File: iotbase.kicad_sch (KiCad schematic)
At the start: 35 parts, among them J1 USB_C_Receptacle_USB2.0, J2 RCWL-0516, J3 HSPI, J4 VSPI, SW1 Reset, SW2 Boot, U1 AMS1117-3.3, U2 Connector_IoT_GPIO, U3 ESP32-WROOM-E, U4 BME280, U6 Connector_ESProg, U7 Connector_I2C, U8 Connector_I2C

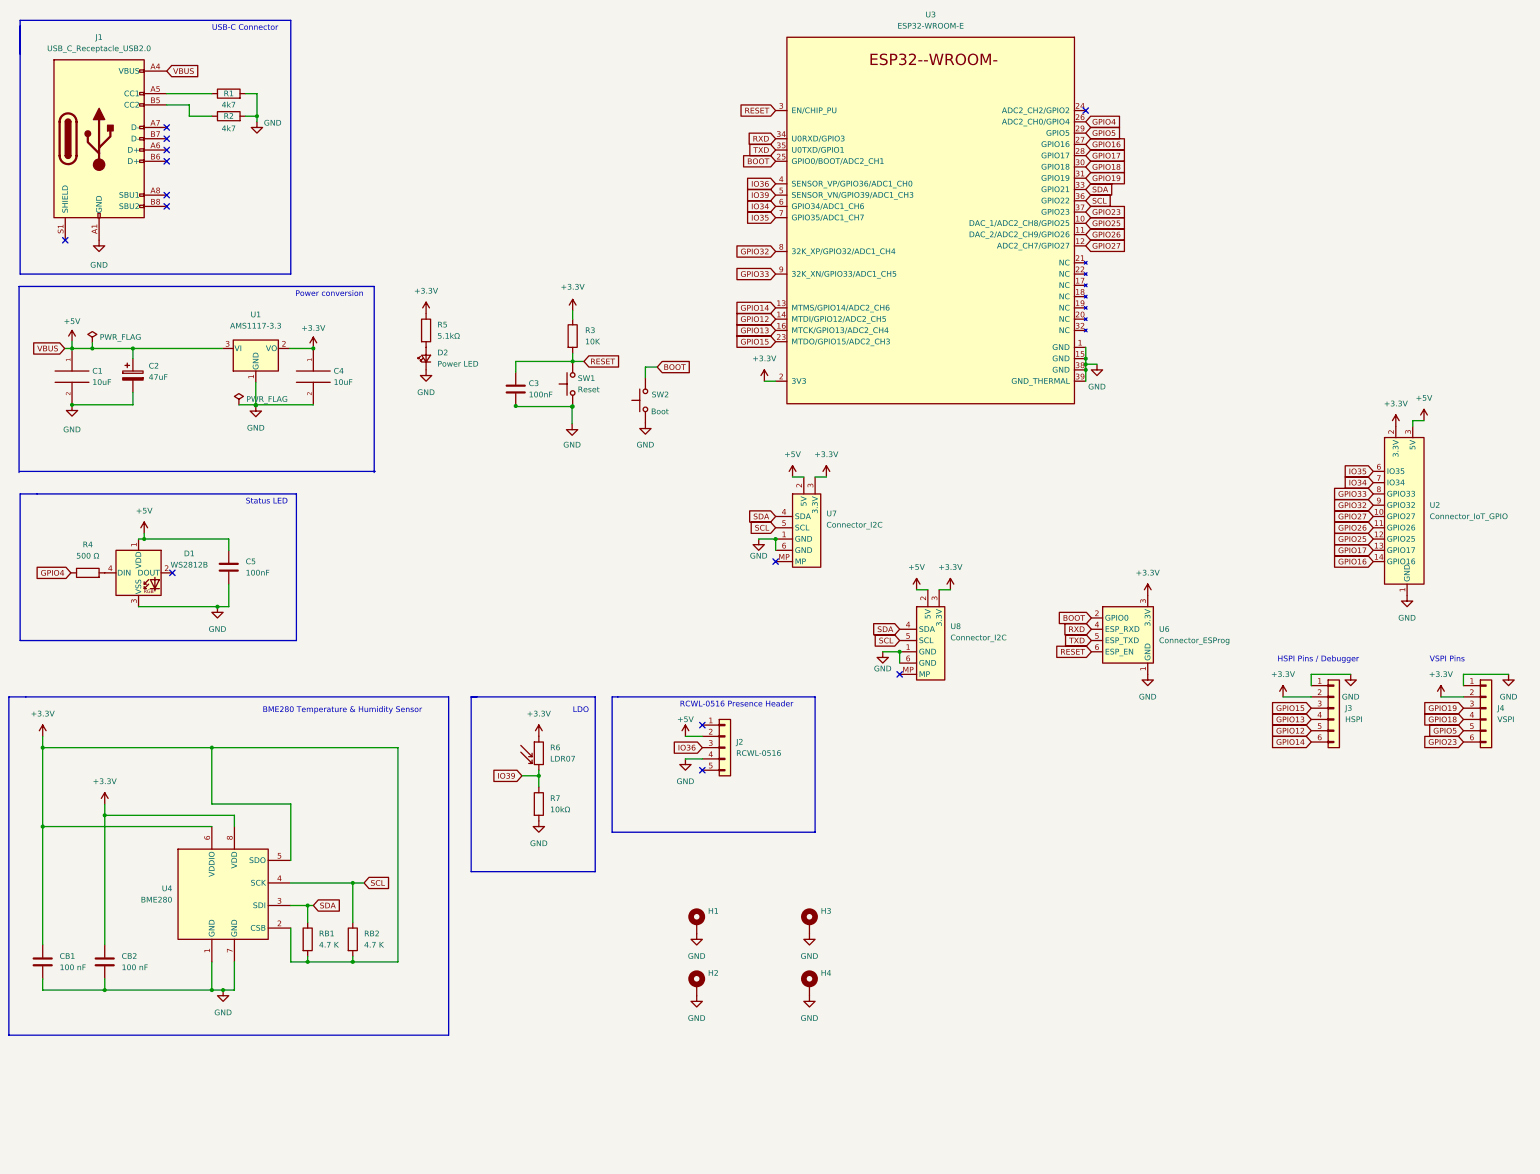
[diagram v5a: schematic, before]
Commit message: updated components and layout.
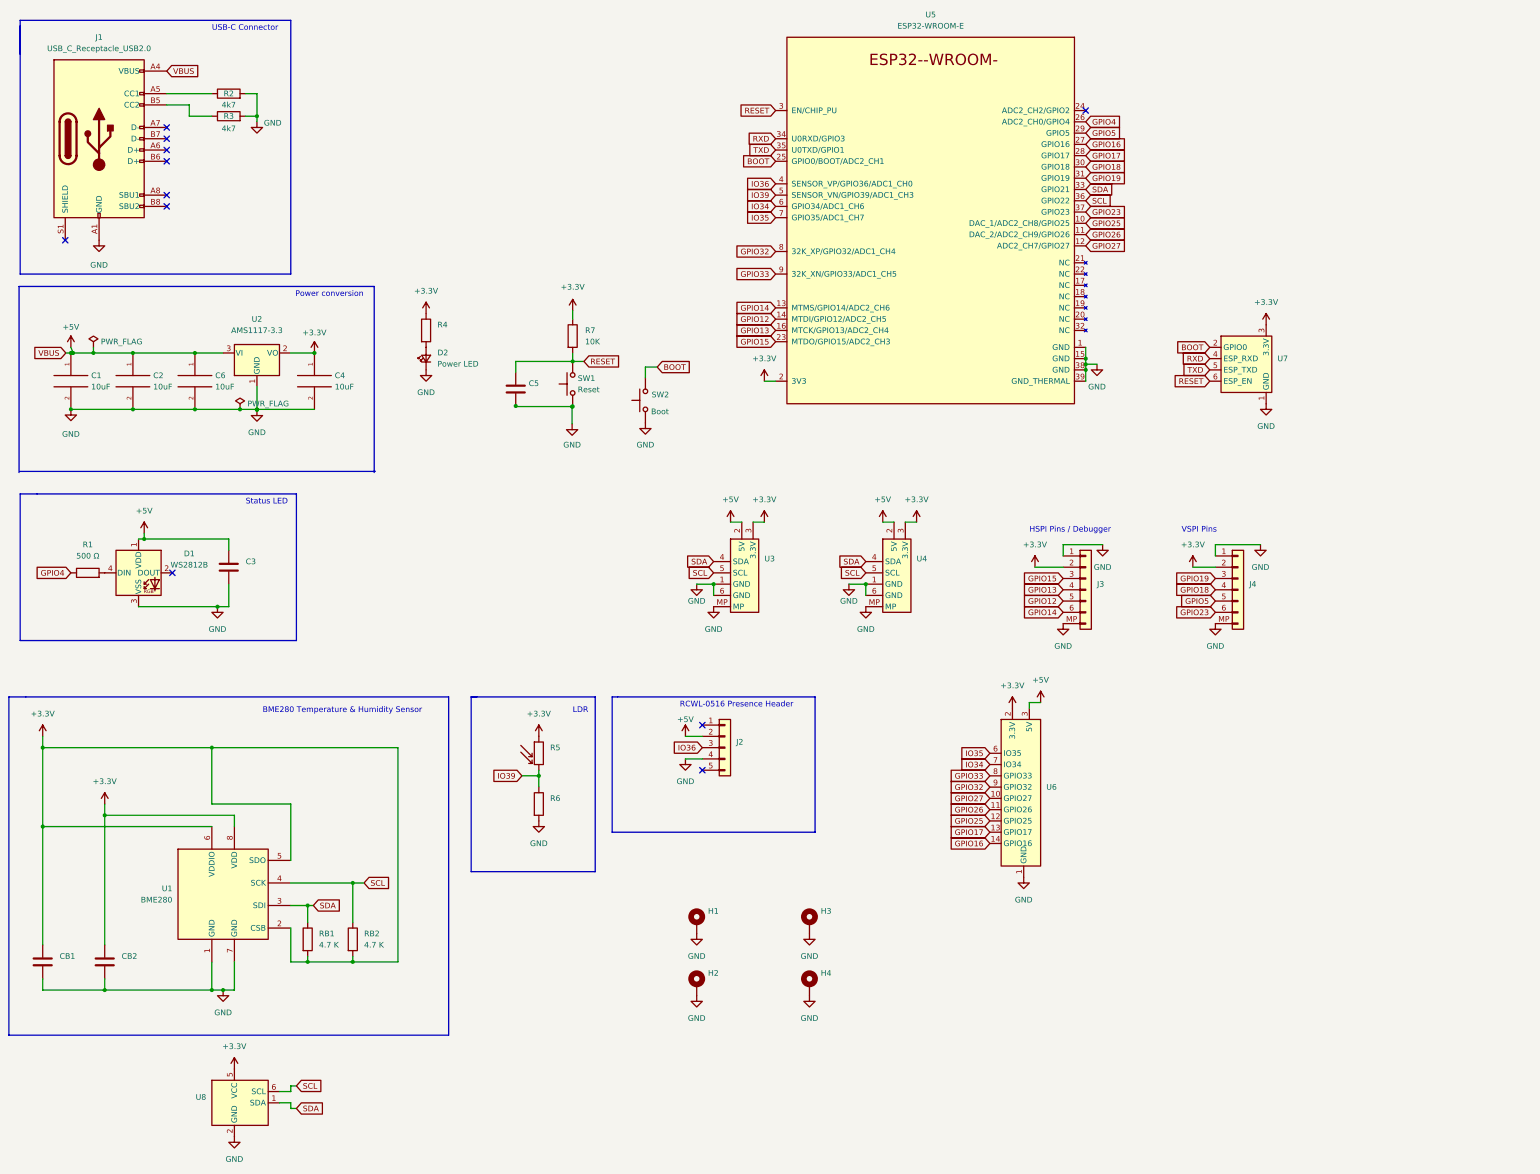
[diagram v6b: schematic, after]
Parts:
- removed C2: 47uF, Capacitor_SMD:C_1206_3216Metric, symbol Device:C_Polarized
- removed J3: HSPI, Connector_JST:JST_SH_BM06B-SRSS-TB_1x06-1MP_P1.00mm_Vertical, symbol Connector_Generic:Conn_01x06
- removed J4: VSPI, Connector_JST:JST_SH_BM06B-SRSS-TB_1x06-1MP_P1.00mm_Vertical, symbol Connector_Generic:Conn_01x06
- added C2, C6: 10uF, Capacitor_SMD:C_0603_1608Metric, symbol pspice:CAP
- added J3, J4: (no value), symbol Connector_Generic:Conn_01x07
- added U8: (no value), symbol Sensor_Humidity:HDC1080
- C3: renamed from C5; value 100nF -> (none); footprint Resistor_SMD:R_0603_1608Metric -> (none)
- C5: renamed from C3; value 100nF -> (none); footprint Resistor_SMD:R_0603_1608Metric -> (none)
- CB1, CB2: value 100 nF -> (none)
- J2: value RCWL-0516 -> (none); footprint 0_Project:PinHeader_RCWL-0516 -> (none); now left out of the parts list
- R4: renamed from R5; value 5.1kΩ -> (none)
- R5: renamed from R6; value LDR07 -> (none); footprint OptoDevice:R_LDR_5.1x4.3mm_P3.4mm_Vertical -> (none); now left out of the parts list
- R6: renamed from R7; value 10kΩ -> (none)
- U3: renamed from U7; value Connector_I2C -> (none); footprint Connector_JST:JST_SH_BM06B-SRSS-TB_1x06-1MP_P1.00mm_Vertical -> (none); now left out of the parts list
- U4: renamed from U8; value Connector_I2C -> (none); footprint Connector_JST:JST_SH_BM06B-SRSS-TB_1x06-1MP_P1.00mm_Vertical -> (none); now left out of the parts list
- U6: renamed from U2; value Connector_IoT_GPIO -> (none); footprint 0_Project:Connector_IoT_GPIO -> (none)
- U7: renamed from U6; value Connector_ESProg -> (none); footprint Connector:Tag-Connect_TC2030-IDC-FP_2x03_P1.27mm_Vertical -> (none); now left out of the parts list
- renumbered R4 to R1, R1 to R2, R2 to R3, R3 to R7, U4 to U1, U1 to U2, U3 to U5
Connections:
- net +3V3: now also J3.2 (Pin_2), J4.2 (Pin_2), U8.5 (VCC)
- net +5V: now also C2.1, C6.1
- net GND: now also U3.MP, U4.MP, C2.2, C6.2, J3.1 (Pin_1), J3.MP, J4.1 (Pin_1), J4.MP, U8.2 (GND)
- net GPIO12: now also J3.5 (Pin_5)
- net GPIO13: now also J3.4 (Pin_4)
- net GPIO14: now also J3.6 (Pin_6)
- net GPIO15: now also J3.3 (Pin_3)
- net GPIO18: now also J4.4 (Pin_4)
- net GPIO19: now also J4.3 (Pin_3)
- net GPIO23: now also J4.6 (Pin_6)
- net GPIO5: now also J4.5 (Pin_5)
- net SCL: now also U8.6 (SCL)
- net SDA: now also U8.1 (SDA)
- no-connect marks 13 -> 11
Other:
- note added: "LDR"
- note removed: "LDO"
- moved on the sheet: C1, C4, U2, U3, U4, U6, U7

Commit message: adds rounded corners adds connector pin silkscreens
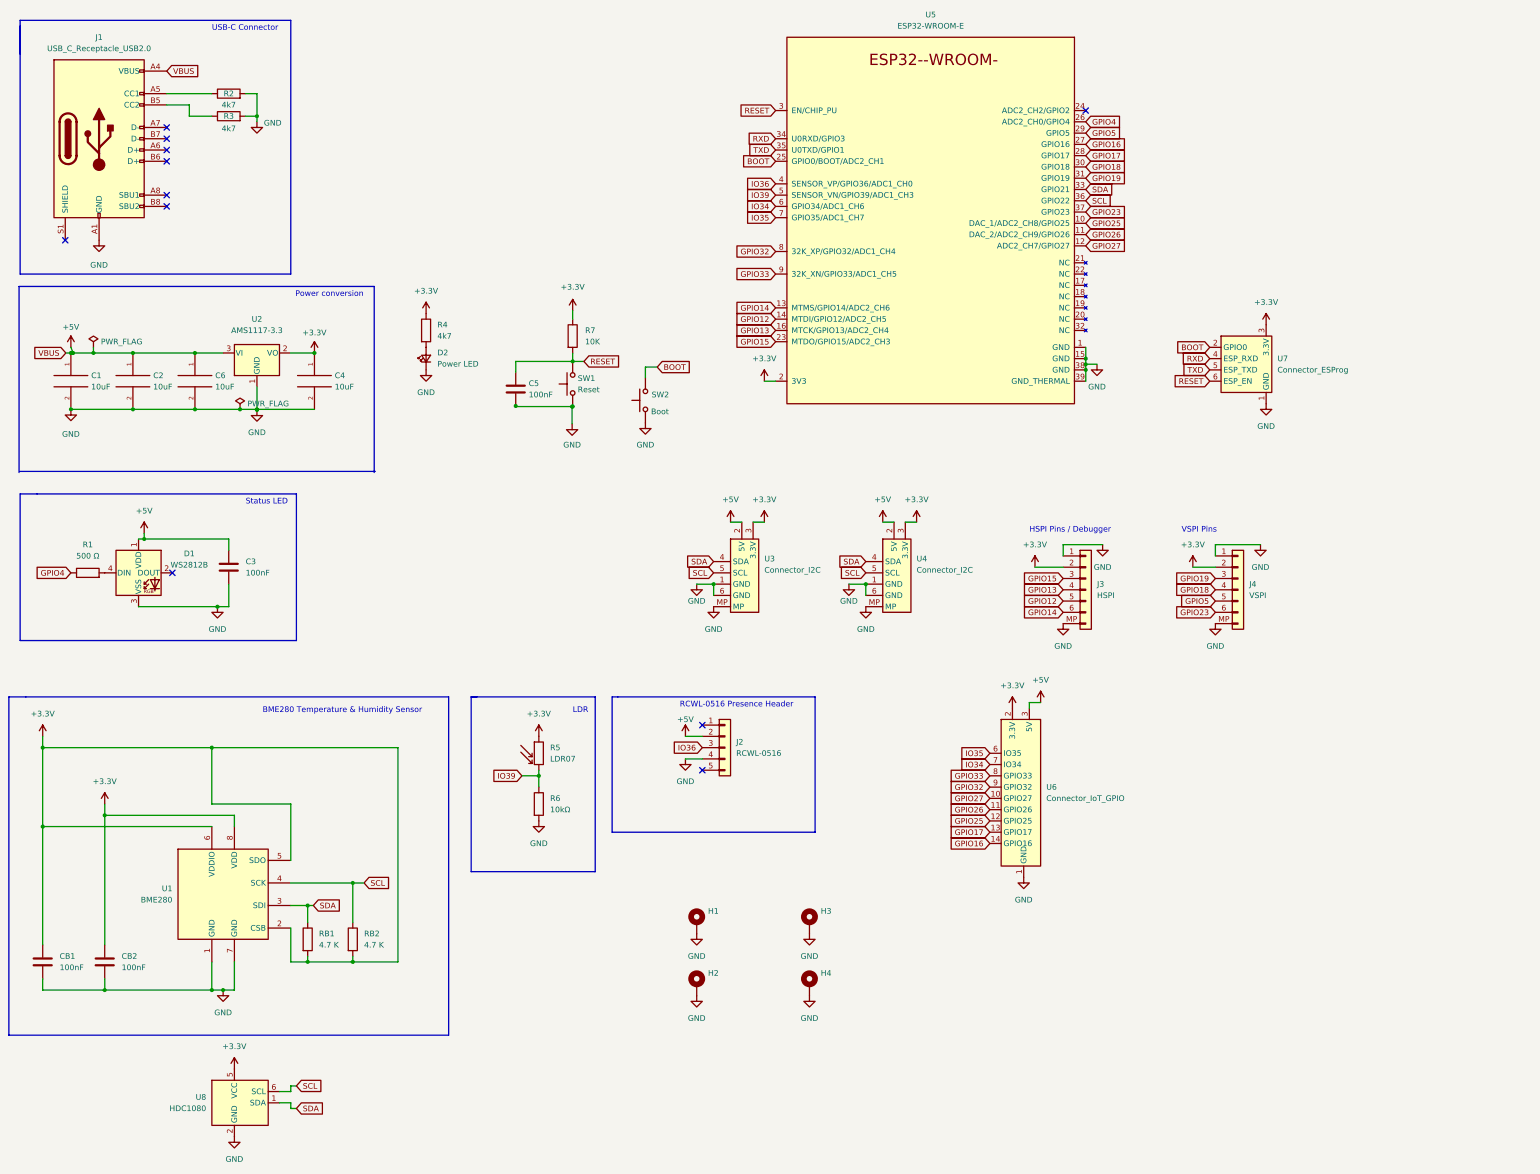
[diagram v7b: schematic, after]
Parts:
- C3, C5: value (none) -> 100nF; footprint (none) -> Capacitor_SMD:C_0603_1608Metric
- CB1, CB2: value (none) -> 100nF
- J2: value (none) -> RCWL-0516; footprint (none) -> 0_Project:PinHeader_RCWL-0516
- J3: value (none) -> HSPI; footprint (none) -> Connector_JST:JST_SH_BM06B-SRSS-TB_1x06-1MP_P1.00mm_Vertical
- J4: value (none) -> VSPI; footprint (none) -> Connector_JST:JST_SH_BM06B-SRSS-TB_1x06-1MP_P1.00mm_Vertical
- R4: value (none) -> 4k7
- R5: value (none) -> LDR07; footprint (none) -> OptoDevice:R_LDR_5.1x4.3mm_P3.4mm_Vertical
- R6: value (none) -> 10kΩ
- U3, U4: value (none) -> Connector_I2C; footprint (none) -> Connector_JST:JST_SH_BM06B-SRSS-TB_1x06-1MP_P1.00mm_Vertical
- U6: value (none) -> Connector_IoT_GPIO; footprint (none) -> 0_Project:Connector_IoT_GPIO
- U7: value (none) -> Connector_ESProg; footprint (none) -> Connector:Tag-Connect_TC2030-IDC-FP_2x03_P1.27mm_Vertical
- U8: value (none) -> HDC1080; footprint (none) -> Package_SON:Texas_PWSON-N6
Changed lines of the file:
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@@
       (effects (font (size 1.27 1.27)) (justify left))
     )
-    (property "Value" "" (id 1) (at 38.1 229.8699 0)
+    (property "Value" "100nF" (id 1) (at 38.1 229.8699 0)
       (effects (font (size 1.27 1.27)) (justify left))
     )
@@
       (effects (font (size 1.27 1.27)) (justify left))
     )
-    (property "Value" "" (id 1) (at 190.5 181.6099 0)
-      (effects (font (size 1.27 1.27)) (justify left))
-    )
-    (property "Footprint" "" (id 2) (at 187.96 180.34 0)
+    (property "Value" "RCWL-0516" (id 1) (at 190.5 181.6099 0)
+      (effects (font (size 1.27 1.27)) (justify left))
+    )
+    (property "Footprint" "0_Project:PinHeader_RCWL-0516" (id 2) (at 187.96 180.34 0)
       (effects (font (size 1.27 1.27)) hide)
     )
@@
       (effects (font (size 1.27 1.27)) (justify right))
     )
-    (property "Value" "" (id 1) (at 71.12 261.6199 0)
+    (property "Value" "HDC1080" (id 1) (at 71.12 261.6199 0)
       (effects (font (size 1.27 1.27)) (justify right))
     )
-    (property "Footprint" "" (id 2) (at 78.74 266.7 0)
+    (property "Footprint" "Package_SON:Texas_PWSON-N6" (id 2) (at 78.74 266.7 0)
       (effects (font (size 1.27 1.27)) (justify left) hide)
     )
@@
       (effects (font (size 1.27 1.27)) (justify left))
     )
-    (property "Value" "" (id 1) (at 231.14 140.3349 0)
-      (effects (font (size 1.27 1.27)) (justify left))
-    )
-    (property "Footprint" "" (id 2) (at 224.79 133.35 0)
+    (property "Value" "Connector_I2C" (id 1) (at 231.14 140.3349 0)
+      (effects (font (size 1.27 1.27)) (justify left))
+    )
+    (property "Footprint" "Connector_JST:JST_SH_BM06B-SRSS-TB_1x06-1MP_P1.00mm_Vertical" (id 2) (at 224.79 133.35 0)
       (effects (font (size 1.27 1.27)) hide)
     )
@@
       (effects (font (size 1.27 1.27)) (justify left))
     )
-    (property "Value" "" (id 1) (at 260.35 191.7699 0)
-      (effects (font (size 1.27 1.27)) (justify left))
-    )
-    (property "Footprint" "" (id 2) (at 254 156.21 0)
+    (property "Value" "Connector_IoT_GPIO" (id 1) (at 260.35 191.7699 0)
+      (effects (font (size 1.27 1.27)) (justify left))
+    )
+    (property "Footprint" "0_Project:Connector_IoT_GPIO" (id 2) (at 254 156.21 0)
       (effects (font (size 1.27 1.27)) hide)
     )
@@
       (effects (font (size 1.27 1.27)) (justify left))
     )
-    (property "Value" "" (id 1) (at 148.59 194.3099 0)
+    (property "Value" "10kΩ" (id 1) (at 148.59 194.3099 0)
       (effects (font (size 1.27 1.27)) (justify left))
     )
@@
       (effects (font (size 1.27 1.27)) (justify left))
     )
-    (property "Value" "" (id 1) (at 148.59 182.8799 0)
-      (effects (font (size 1.27 1.27)) (justify left))
-    )
-    (property "Footprint" "" (id 2) (at 150.495 181.61 90)
+    (property "Value" "LDR07" (id 1) (at 148.59 182.8799 0)
+      (effects (font (size 1.27 1.27)) (justify left))
+    )
+    (property "Footprint" "OptoDevice:R_LDR_5.1x4.3mm_P3.4mm_Vertical" (id 2) (at 150.495 181.61 90)
       (effects (font (size 1.27 1.27)) hide)
     )
@@
       (effects (font (size 1.27 1.27)) (justify left))
     )
-    (property "Value" "" (id 1) (at 312.42 95.2499 0)
-      (effects (font (size 1.27 1.27)) (justify left))
-    )
-    (property "Footprint" "" (id 2) (at 304.8 83.82 0)
+    (property "Value" "Connector_ESProg" (id 1) (at 312.42 95.2499 0)
+      (effects (font (size 1.27 1.27)) (justify left))
+    )
+    (property "Footprint" "Connector:Tag-Connect_TC2030-IDC-FP_2x03_P1.27mm_Vertical" (id 2) (at 304.8 83.82 0)
       (effects (font (size 1.27 1.27)) hide)
     )
@@
       (effects (font (size 1.27 1.27)) (justify left))
     )
-    (property "Value" "" (id 1) (at 196.85 140.3349 0)
-      (effects (font (size 1.27 1.27)) (justify left))
-    )
-    (property "Footprint" "" (id 2) (at 190.5 133.35 0)
+    (property "Value" "Connector_I2C" (id 1) (at 196.85 140.3349 0)
+      (effects (font (size 1.27 1.27)) (justify left))
+    )
+    (property "Footprint" "Connector_JST:JST_SH_BM06B-SRSS-TB_1x06-1MP_P1.00mm_Vertical" (id 2) (at 190.5 133.35 0)
       (effects (font (size 1.27 1.27)) hide)
     )
@@
       (effects (font (size 1.27 1.27)) (justify left))
     )
-    (property "Value" "" (id 1) (at 271.78 146.0499 0)
-      (effects (font (size 1.27 1.27)) (justify left))
-    )
-    (property "Footprint" "" (id 2) (at 269.24 144.78 0)
+    (property "Value" "HSPI" (id 1) (at 271.78 146.0499 0)
+      (effects (font (size 1.27 1.27)) (justify left))
+    )
+    (property "Footprint" "Connector_JST:JST_SH_BM06B-SRSS-TB_1x06-1MP_P1.00mm_Vertical" (id 2) (at 269.24 144.78 0)
       (effects (font (size 1.27 1.27)) hide)
     )
@@
       (effects (font (size 1.27 1.27)) (justify left))
     )
-    (property "Value" "" (id 1) (at 52.07 229.8699 0)
+    (property "Value" "100nF" (id 1) (at 52.07 229.8699 0)
       (effects (font (size 1.27 1.27)) (justify left))
     )
@@
       (effects (font (size 1.27 1.27)) (justify left))
     )
-    (property "Value" "" (id 1) (at 80.01 140.9699 0)
-      (effects (font (size 1.27 1.27)) (justify left))
-    )
-    (property "Footprint" "" (id 2) (at 77.1652 143.51 0)
+    (property "Value" "100nF" (id 1) (at 80.01 140.9699 0)
+      (effects (font (size 1.27 1.27)) (justify left))
+    )
+    (property "Footprint" "Capacitor_SMD:C_0603_1608Metric" (id 2) (at 77.1652 143.51 0)
       (effects (font (size 1.27 1.27)) hide)
     )
@@
       (effects (font (size 1.27 1.27)) (justify left))
     )
-    (property "Value" "" (id 1) (at 123.19 87.6299 0)
+    (property "Value" "4k7" (id 1) (at 123.19 87.6299 0)
       (effects (font (size 1.27 1.27)) (justify left))
     )
@@
       (effects (font (size 1.27 1.27)) (justify left))
     )
-    (property "Value" "" (id 1) (at 143.764 100.8379 0)
-      (effects (font (size 1.27 1.27)) (justify left))
-    )
-    (property "Footprint" "" (id 2) (at 141.8082 103.378 0)
+    (property "Value" "100nF" (id 1) (at 143.764 100.8379 0)
+      (effects (font (size 1.27 1.27)) (justify left))
+    )
+    (property "Footprint" "Capacitor_SMD:C_0603_1608Metric" (id 2) (at 141.8082 103.378 0)
       (effects (font (size 1.27 1.27)) hide)
     )
@@
       (effects (font (size 1.27 1.27)) (justify left))
     )
-    (property "Value" "" (id 1) (at 306.07 146.0499 0)
-      (effects (font (size 1.27 1.27)) (justify left))
-    )
-    (property "Footprint" "" (id 2) (at 303.53 144.78 0)
-      (effects (font (size 1.27 1.27)) hide)
-    )
+    (property "Value" "VSPI" (id 1) (at 306.07 146.0499 0)
+      (effects (font (size 1.27 1.27)) (justify left))
+    )
+    (property "Footprint" "Connector_JST:JST_SH_BM06B-SRSS-TB_1x06-1MP_P1.00mm_Vertical" (id 2) (at 303.53 144.78 0)
+      (effects (font (size 1.27 1.27)) hide)
+    )
